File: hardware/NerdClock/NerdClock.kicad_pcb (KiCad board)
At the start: 2 copper layers, 123 x 123 mm, 100 parts, among them J1 Conn_01x02, J10 Conn_01x04, J11 Conn_01x02, J12 Conn_01x02, J2 Jack-DC, J3 ICSP, J4 Conn_01x04, J5 Conn_01x02, J6 Conn_01x02, J7 USB_B_Micro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

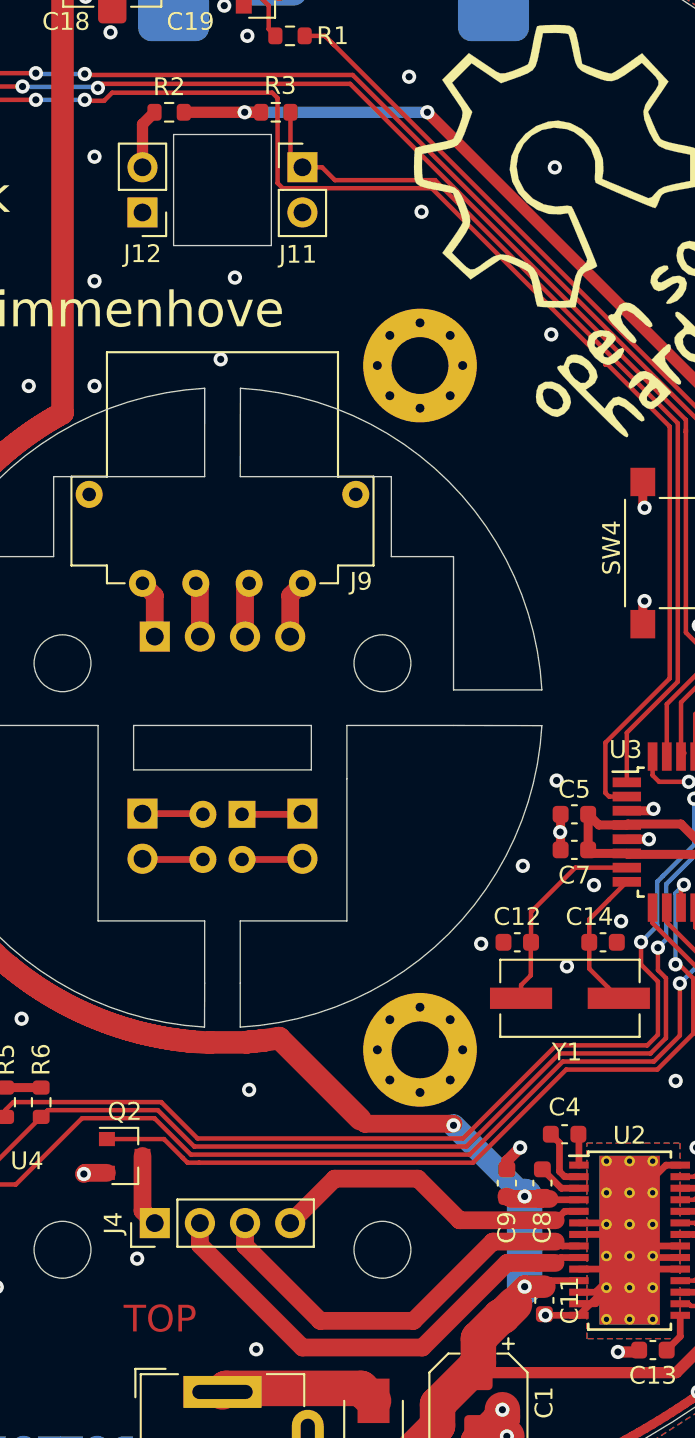
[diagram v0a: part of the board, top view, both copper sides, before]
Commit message: Fixed hardware bug (polarity of IR led in relfection sensor
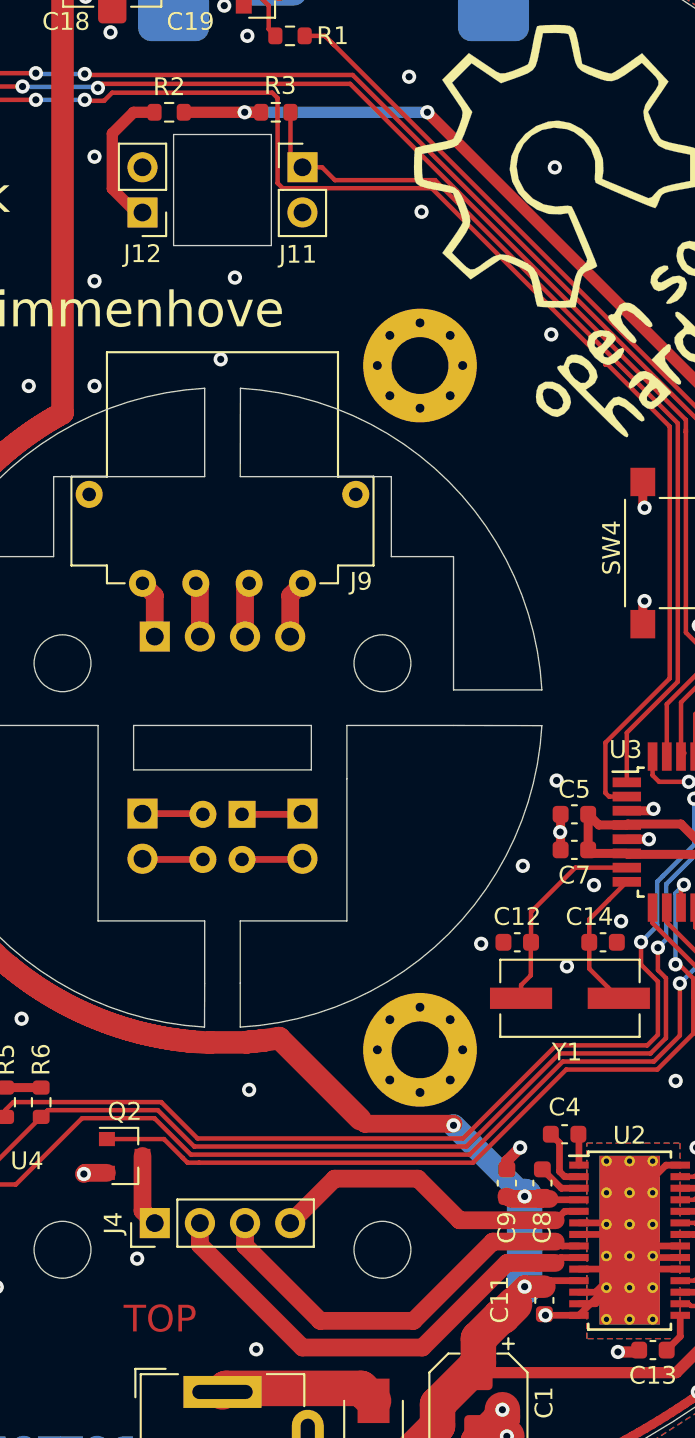
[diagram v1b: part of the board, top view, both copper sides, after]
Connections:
- J12 pad 1: GND -> Net-(J12-Pad1)
- J12 pad 2: Net-(J12-Pad2) -> GND
- R2 pad 1: Net-(J12-Pad2) -> Net-(J12-Pad1)
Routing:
- net Net-(J12-Pad1): track 0.00 -> 8.23 mm
- net Net-(J12-Pad2): track 3.38 -> 0.00 mm
